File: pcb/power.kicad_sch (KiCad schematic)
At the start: 7 parts, among them U4 LP3993-33B3F

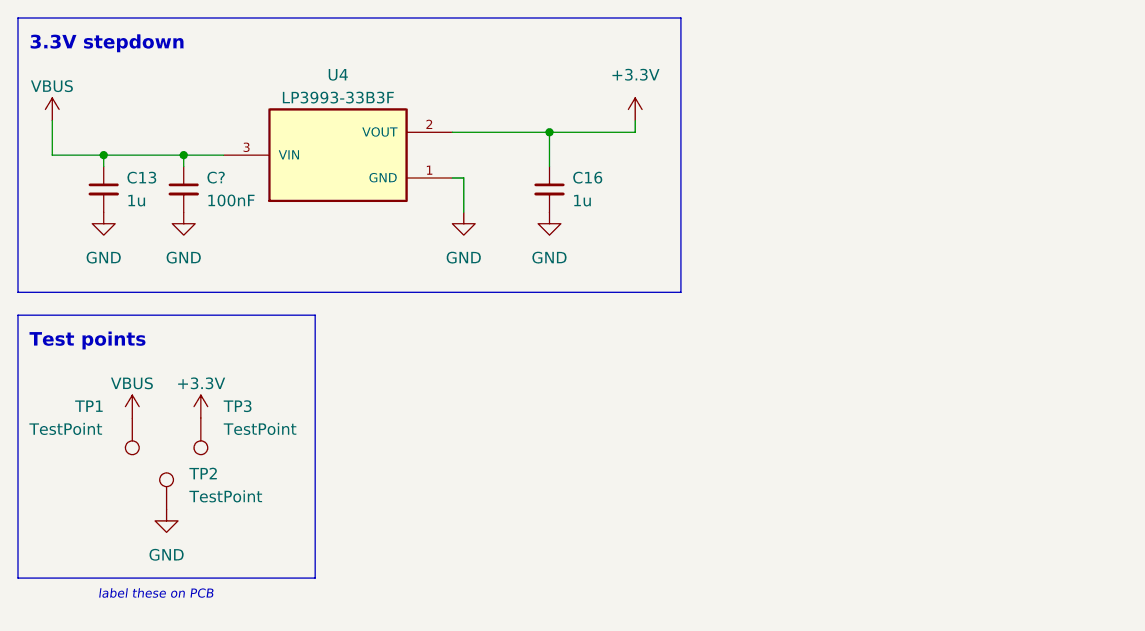
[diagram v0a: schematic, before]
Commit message: Finished off schematic
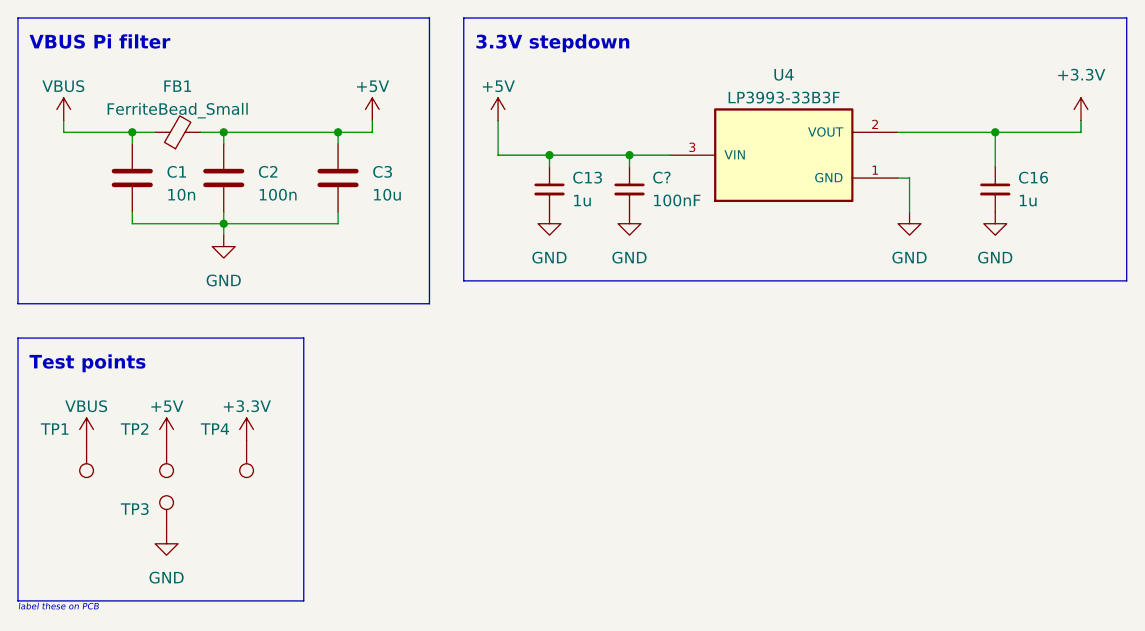
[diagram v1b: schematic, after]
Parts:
- added C1: 10n, symbol Device:C
- added C2: 100n, symbol Device:C
- added C3: 10u, symbol Device:C
- added FB1: FerriteBead_Small, Inductor_SMD:L_0201_0603Metric, symbol Device:FerriteBead_Small
- added TP2: ~, TestPoint:TestPoint_Pad_D2.0mm, symbol Connector:TestPoint
- TP1: value TestPoint -> ~
- TP3: renamed from TP2; value TestPoint -> ~
- TP4: renamed from TP3; value TestPoint -> ~
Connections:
- net GND: now also C1.2, C2.2, C3.2
- net VBUS: now also C1.1, FB1.1; no longer C13.1, C?.1, U4.3 (VIN)
- new net +5V: C13.1, C2.1, C3.1, C?.1, FB1.2, TP2.1, U4.3 (VIN)
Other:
- note added: "VBUS Pi filter"
- moved on the sheet: C13, C16, C?, TP1, TP3, TP4, U4

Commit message: Fixed up footprints, added readme
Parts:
- C1, C2: footprint (none) -> Capacitor_SMD:C_0201_0603Metric
- C13, C16: footprint Capacitor_SMD:C_0402_1005Metric -> Capacitor_SMD:C_0201_0603Metric
- C3: footprint (none) -> Capacitor_SMD:C_0805_2012Metric; LCSC (none) -> C396720
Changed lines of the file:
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@@
       (effects (font (size 1.27 1.27)) (justify left))
     )
-    (property "Footprint" "" (at 39.0652 46.99 0)
+    (property "Footprint" "Capacitor_SMD:C_0201_0603Metric" (at 39.0652 46.99 0)
       (effects (font (size 1.27 1.27)) hide)
     )
@@
       (effects (font (size 1.27 1.27)) (justify left))
     )
-    (property "Footprint" "" (at 61.9252 46.99 0)
+    (property "Footprint" "Capacitor_SMD:C_0805_2012Metric" (at 61.9252 46.99 0)
       (effects (font (size 1.27 1.27)) hide)
     )
     (property "Datasheet" "~" (at 60.96 43.18 0)
+      (effects (font (size 1.27 1.27)) hide)
+    )
+    (property "LCSC" "C396720" (at 60.96 43.18 0)
       (effects (font (size 1.27 1.27)) hide)
     )
@@
       (effects (font (size 1.27 1.27)) (justify right))
     )
-    (property "Footprint" "Capacitor_SMD:C_0402_1005Metric" (at 133.985 44.45 0)
+    (property "Footprint" "Capacitor_SMD:C_0201_0603Metric" (at 133.985 44.45 0)
       (effects (font (size 1.27 1.27)) hide)
     )
@@
       (effects (font (size 1.27 1.27)) (justify right))
     )
-    (property "Footprint" "Capacitor_SMD:C_0402_1005Metric" (at 84.455 44.45 0)
+    (property "Footprint" "Capacitor_SMD:C_0201_0603Metric" (at 84.455 44.45 0)
       (effects (font (size 1.27 1.27)) hide)
     )
@@
       (effects (font (size 1.27 1.27)) (justify left))
     )
-    (property "Footprint" "" (at 49.2252 46.99 0)
-      (effects (font (size 1.27 1.27)) hide)
-    )
+    (property "Footprint" "Capacitor_SMD:C_0201_0603Metric" (at 49.2252 46.99 0)
+      (effects (font (size 1.27 1.27)) hide)
+    )

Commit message: Started routing
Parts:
- C1, C13, C16, C2: footprint Capacitor_SMD:C_0201_0603Metric -> Capacitor_SMD:C_0603_1608Metric
- FB1: footprint Inductor_SMD:L_0201_0603Metric -> Inductor_SMD:L_0603_1608Metric
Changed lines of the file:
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@@
       (effects (font (size 1.27 1.27)) (justify left))
     )
-    (property "Footprint" "Capacitor_SMD:C_0201_0603Metric" (at 39.0652 46.99 0)
+    (property "Footprint" "Capacitor_SMD:C_0603_1608Metric" (at 39.0652 46.99 0)
       (effects (font (size 1.27 1.27)) hide)
     )
@@
       (effects (font (size 1.27 1.27)) (justify right))
     )
-    (property "Footprint" "Capacitor_SMD:C_0201_0603Metric" (at 133.985 44.45 0)
+    (property "Footprint" "Capacitor_SMD:C_0603_1608Metric" (at 133.985 44.45 0)
       (effects (font (size 1.27 1.27)) hide)
     )
@@
       (effects (font (size 1.27 1.27)) (justify right))
     )
-    (property "Footprint" "Capacitor_SMD:C_0201_0603Metric" (at 84.455 44.45 0)
+    (property "Footprint" "Capacitor_SMD:C_0603_1608Metric" (at 84.455 44.45 0)
       (effects (font (size 1.27 1.27)) hide)
     )
@@
       (effects (font (size 1.27 1.27)) (justify left))
     )
-    (property "Footprint" "Capacitor_SMD:C_0201_0603Metric" (at 49.2252 46.99 0)
+    (property "Footprint" "Capacitor_SMD:C_0603_1608Metric" (at 49.2252 46.99 0)
       (effects (font (size 1.27 1.27)) hide)
     )
@@
       (effects (font (size 1.27 1.27)))
     )
-    (property "Footprint" "Inductor_SMD:L_0201_0603Metric" (at 43.18 39.878 90)
-      (effects (font (size 1.27 1.27)) hide)
-    )
+    (property "Footprint" "Inductor_SMD:L_0603_1608Metric" (at 43.18 39.878 90)
+      (effects (font (size 1.27 1.27)) hide)
+    )
